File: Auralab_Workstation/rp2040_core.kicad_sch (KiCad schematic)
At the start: 0 parts

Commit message: started with connectionns
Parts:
- added C1: 1uF, symbol Device:C
- added C2, C3, C4: 100nF, symbol Device:C
- added U1: RP2040, Package_DFN_QFN:QFN-56-1EP_7x7mm_P0.4mm_EP3.2x3.2mm, symbol MCU_RaspberryPi:RP2040
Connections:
- new net +3.3V: C2.1, C3.1, C4.1, U1.1 (IOVDD), U1.10 (IOVDD), U1.22 (IOVDD), U1.33 (IOVDD), U1.42 (IOVDD), U1.44 (VREG_IN), U1.48 (USB_VDD), U1.49 (IOVDD)
- new net GND: C1.2, C2.2, C3.2, C4.2
- new net V1_CORE: C1.1, U1.23 (DVDD), U1.45 (VREG_VOUT), U1.50 (DVDD)

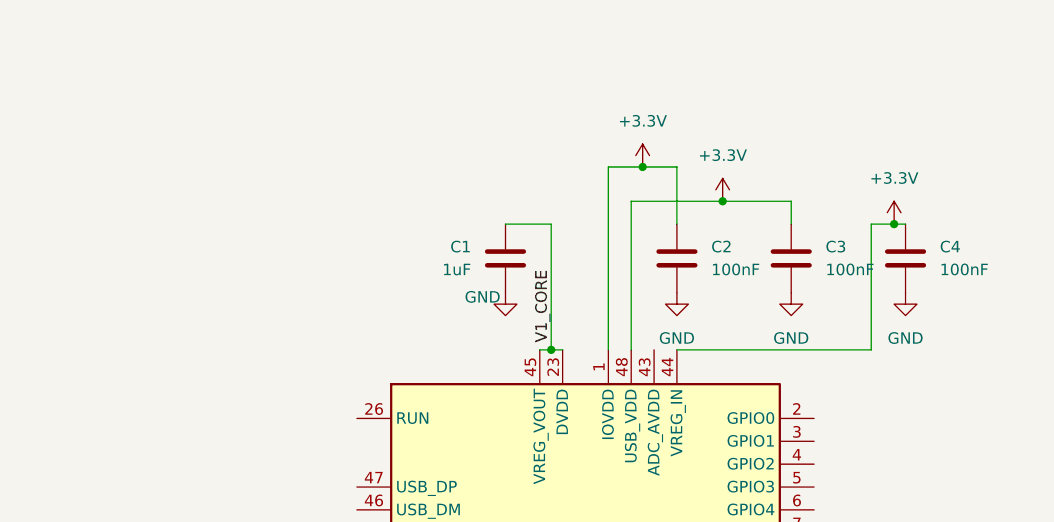
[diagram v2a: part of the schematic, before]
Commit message: just rotated one net label in ur sch
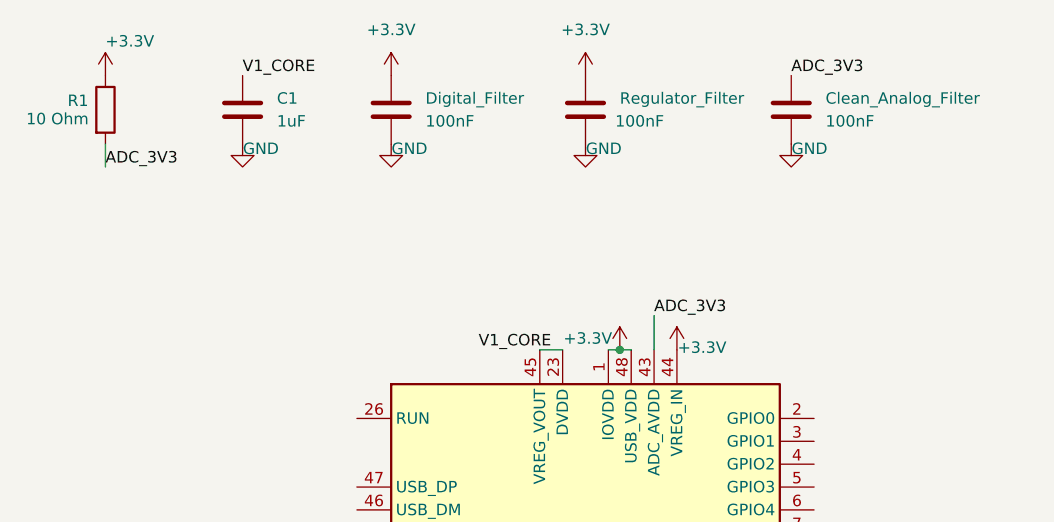
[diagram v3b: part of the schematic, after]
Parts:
- removed C2, C3, C4: 100nF, symbol Device:C
- added Clean_Analog_Filter, Digital_Filter, Regulator_Filter: 100nF, symbol Device:C
- added R1: 10 Ohm, symbol Device:R
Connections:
- net +3.3V: now also Digital_Filter.1, R1.1, Regulator_Filter.1
- net GND: now also Clean_Analog_Filter.2, Digital_Filter.2, Regulator_Filter.2
- net ADC_3V3: now reaches U1.43 (ADC_AVDD)
- net ADC_3V3: now also Clean_Analog_Filter.1, R1.2

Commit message: oralavu panirken rp2040, nect un connections and mine sekanom that i will do tmrw
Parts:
- added C2, C3: 27pF, symbol Device:C
- added C4: 100nF, symbol Device:C
- added R2, R3: 27 Ohm, symbol Device:R
- added U2: W25Q128JVS, Package_SO:SOIC-8_5.3x5.3mm_P1.27mm, symbol Memory_Flash:W25Q128JVS
- added Y1: Crystal_GND24, symbol Device:Crystal_GND24
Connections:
- net +3.3V: now also C4.1, U2.8 (VCC)
- net GND: now also C2.2, C3.2, C4.2, U2.4 (GND)
- net XIN: now reaches U1.20 (XIN)
- net XIN: now also C2.1, Y1.1
- net XOUT: now reaches U1.21 (XOUT)
- net XOUT: now also C3.1, Y1.3
- net USB_DM: now reaches U1.46 (USB_DM)
- net USB_DM: now also R3.1
- net USB_DP: now reaches U1.47 (USB_DP)
- net USB_DP: now also R2.1
- net QSPI_IO3: now reaches U1.51 (QSPI_SD3)
- net QSPI_IO3: now also U2.7 (~{HOLD}/~{RESET}/IO_{3})
- net QSPI_CLK: now reaches U1.52 (QSPI_SCLK)
- net QSPI_CLK: now also U2.6 (CLK)
- net QSPI_IO0: now reaches U1.53 (QSPI_SD0)
- net QSPI_IO0: now also U2.5 (DI/IO_{0})
- net QSPI_IO2: now reaches U1.54 (QSPI_SD2)
- net QSPI_IO2: now also U2.3 (~{WP}/IO_{2})
- net QSPI_IO1: now reaches U1.55 (QSPI_SD1)
- net QSPI_IO1: now also U2.2 (DO/IO_{1})
- net QSPI_CS: now reaches U1.56 (QSPI_SS)
- net QSPI_CS: now also U2.1 (~{CS})
- new net USB_D_M: R3.2
- new net USB_D_P: R2.2

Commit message: I almost completed my part ig
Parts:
- added BZ1: Buzzer, symbol Device:Buzzer
- added D1, D2: LED, symbol Device:LED
- added Q1: BC847, Package_TO_SOT_SMD:SOT-23, symbol Transistor_BJT:BC847
- added R4, R6: 220 Ohm, symbol Device:R
- added R5: 1k Ohm, symbol Device:R
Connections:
- net +3.3V: now also U1.26 (RUN), BZ1.1 (+), D1.2 (A)
- net GND: now also U1.57 (GND), Y1.2, Y1.4, Q1.2 (E), R4.1, R6.1
- net BUZZER_CTRL: now reaches U1.11 (GPIO8)
- net BUZZER_CTRL: now also R5.1
- net TFT_SCLK: now reaches U1.27 (GPIO16)
- net TFT_MOSI: now reaches U1.28 (GPIO17)
- net TFT_CS: now reaches U1.29 (GPIO18)
- net TFT_DC: now reaches U1.30 (GPIO19)
- net TFT_RST: now reaches U1.31 (GPIO20)
- net BTN_MENU_NEXT: now reaches U1.32 (GPIO21)
- net BTN_MENU_SELECT: now reaches U1.34 (GPIO22)
- net ALERT_LED: now reaches U1.35 (GPIO23)
- net ALERT_LED: now also D2.2 (A)
- net I2C_SDA: now reaches U1.4 (GPIO2)
- net I2C_SCL: now reaches U1.5 (GPIO3)
- net ADC_SCLK: now reaches U1.6 (GPIO4)
- net ADC_MISO: now reaches U1.7 (GPIO5)
- net ADC_CS: now reaches U1.8 (GPIO6)
- net RANGE_SELECT: now reaches U1.9 (GPIO7)
- net V1_CORE renamed +1.1V
- new net: Q1.1 (B), R5.2
- new net: BZ1.2 (-), Q1.3 (C)
- new net: D1.1 (K), R4.2
- new net: D2.1 (K), R6.2
- no-connect marks 0 -> 18
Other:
- moved on the sheet: C4, U2, Y1
